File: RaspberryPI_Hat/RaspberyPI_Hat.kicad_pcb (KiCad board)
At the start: 2 copper layers, 65 x 56 mm, 17 parts, among them P1 Raspberry_PI, P2 CONN_01X02, P3 UEXT, U1 CAT24C32WI-GT3, U2 TSOP382

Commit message: Добавено реле
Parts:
- added P4: RAS-05-15, myfootprint:RAS-05-15, F.Cu at (107.0, 107.8)
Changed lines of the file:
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@@
 (kicad_pcb (version 4) (host pcbnew 4.0.2-stable)
   (general
-    (links 48)
-    (no_connects 48)
+    (links 44)
+    (no_connects 44)
     (area 97.924999 68.524999 163.075001 124.675001)
     (thickness 1.6)
@@
     (tracks 0)
     (zones 0)
-    (modules 17)
-    (nets 35)
+    (modules 18)
+    (nets 40)
   )
   (page A4)
@@
   (net 33 "Net-(C2-Pad1)")
   (net 34 "Net-(D1-Pad2)")
+  (net 35 "Net-(P4-Pad1)")
+  (net 36 "Net-(P4-Pad2)")
+  (net 37 "Net-(P4-Pad3)")
+  (net 38 "Net-(P4-Pad4)")
+  (net 39 "Net-(P4-Pad5)")
   (net_class Default "This is the default net class."
     (clearance 0.2)
@@
     (add_net "Net-(P1-Pad8)")
     (add_net "Net-(P2-Pad1)")
+    (add_net "Net-(P4-Pad1)")
+    (add_net "Net-(P4-Pad2)")
+    (add_net "Net-(P4-Pad3)")
+    (add_net "Net-(P4-Pad4)")
+    (add_net "Net-(P4-Pad5)")
   )
   (module Mounting_Holes:MountingHole_2.7mm_M2.5_DIN965_Pad (layer F.Cu)
@@
       (net 33 "Net-(C2-Pad1)"))
   )
+  (module myfootprint:RAS-05-15 (layer F.Cu)
+    (at 107 107.85 90)
+    (fp_text reference P4 (at 4.25 7.5 180) (layer F.SilkS)
+      (effects (font (size 1 1) (thickness 0.15)))
+    )
+    (fp_text value RAS-05-15 (at 1.27 -1.27 90) (layer F.Fab)
+      (effects (font (size 1 1) (thickness 0.15)))
+    )
+    (fp_line (start -5.5 15) (end -5.5 0) (layer F.SilkS) (width 0.15))
+    (fp_line (start 15.5 0) (end 15.5 15) (layer F.SilkS) (width 0.15))
+    (fp_line (start -5.5 15) (end 15.5 15) (layer F.SilkS) (width 0.15))
+    (fp_line (start -5.5 0) (end 15.5 0) (layer F.SilkS) (width 0.15))
+    (pad 1 thru_hole circle (at -2.1 1.5 90) (size 2.3 2.3) (drill 1.3) (layers *.Cu *.Mask F.SilkS)
+      (net 35 "Net-(P4-Pad1)"))
+    (pad 2 thru_hole circle (at 10.1 1.5 90) (size 2.3 2.3) (drill 1.3) (layers *.Cu *.Mask F.SilkS)
+      (net 36 "Net-(P4-Pad2)"))
+    (pad 3 thru_hole circle (at -2.1 13.5 90) (size 2.3 2.3) (drill 1.3) (layers *.Cu *.Mask F.SilkS)
+      (net 37 "Net-(P4-Pad3)"))
+    (pad 4 thru_hole circle (at 10.1 13.5 90) (size 2.3 2.3) (drill 1.3) (layers *.Cu *.Mask F.SilkS)
+      (net 38 "Net-(P4-Pad4)"))
+    (pad 5 thru_hole circle (at 12.1 7.5 90) (size 2.3 2.3) (drill 1.3) (layers *.Cu *.Mask F.SilkS)
+      (net 39 "Net-(P4-Pad5)"))
+  )
   (dimension 45 (width 0.3) (layer B.Adhes)

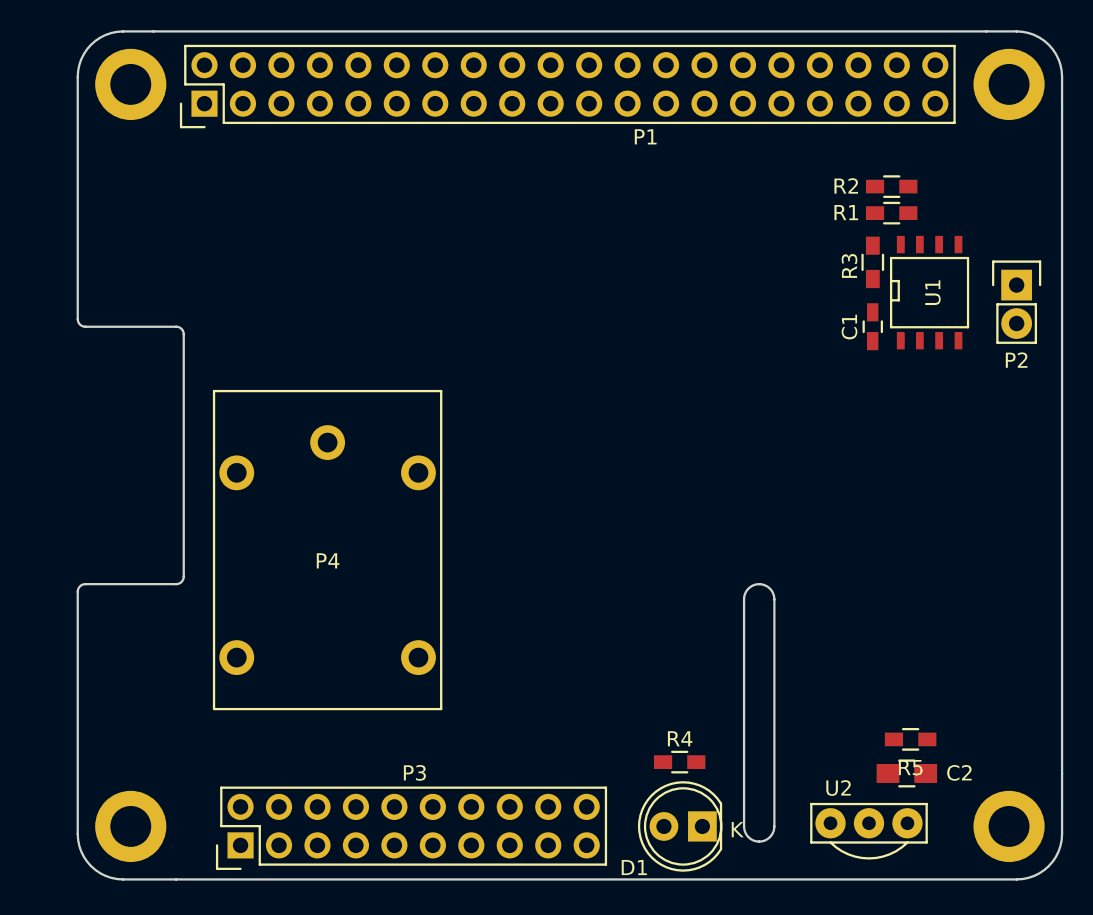
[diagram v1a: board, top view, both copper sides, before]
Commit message: Промяна на UEXT на 2x05 корпус
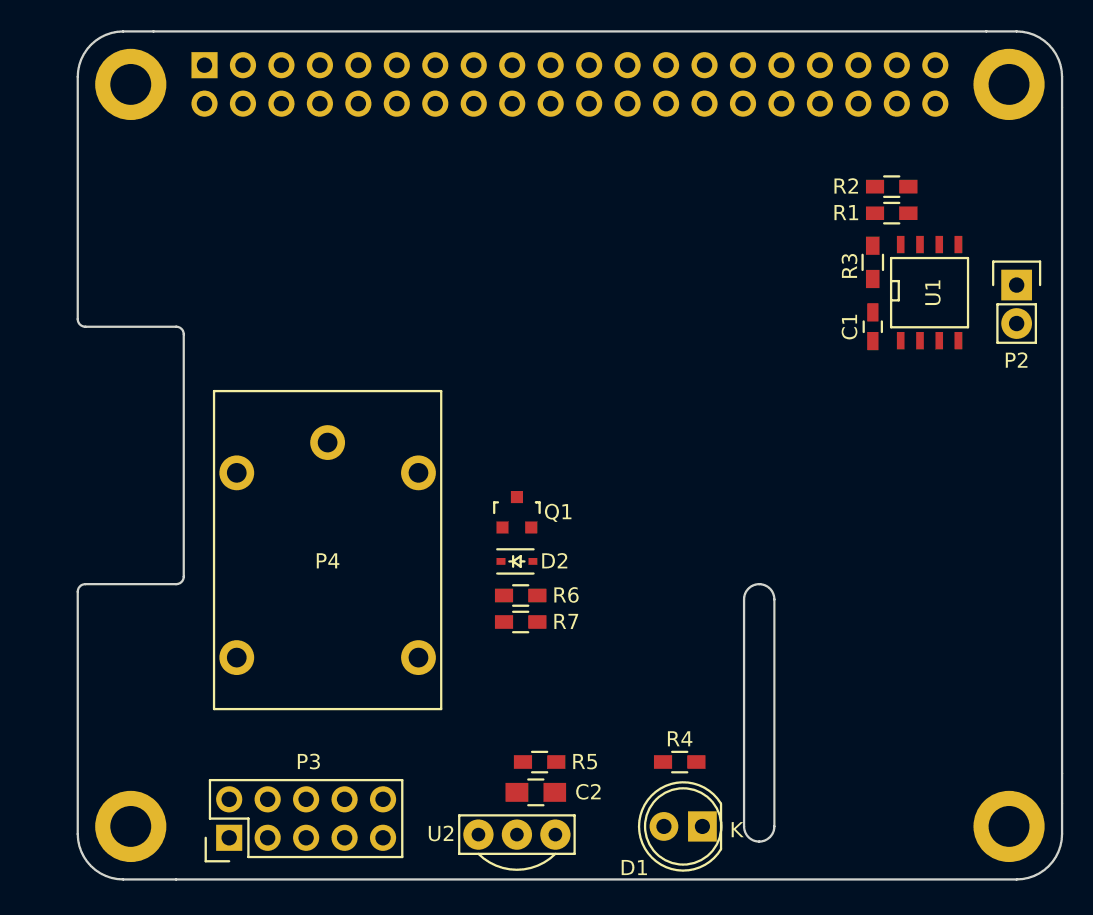
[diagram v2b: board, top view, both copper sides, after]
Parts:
- added D2: 1N4148, Diodes_SMD:SOD-323, F.Cu at (127.0, 103.6)
- added Q1: BC817, TO_SOT_Packages_SMD:SOT-23, F.Cu at (127.0, 100.3)
- added R6: 10K, Resistors_SMD:R_0603_HandSoldering, F.Cu at (127.2, 105.8)
- added R7: 2.2K, Resistors_SMD:R_0603_HandSoldering, F.Cu at (127.2, 107.6)
- C2: value 1.0 -> 10.0
- D1: value IR -> TSAL4600
- P1: moved to B.Cu
- P3: footprint Pin_Headers:Pin_Header_Straight_2x10 -> Pin_Headers:Pin_Header_Straight_2x05
- moved R5 24.5 mm to (128.5, 116.8)
- moved C2 24.5 mm to (128.2, 118.8)
- moved U2 23.3 mm to (127.0, 119.1)
- moved P3 0.90 mm to (108.0, 121.8)
- turned P1 to 270 degrees
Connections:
- P1 pad 2: Net-(P1-Pad2) -> +5V
- P1 pad 4: Net-(P1-Pad4) -> +5V
- P4 pad 2: Net-(P4-Pad2) -> +5V

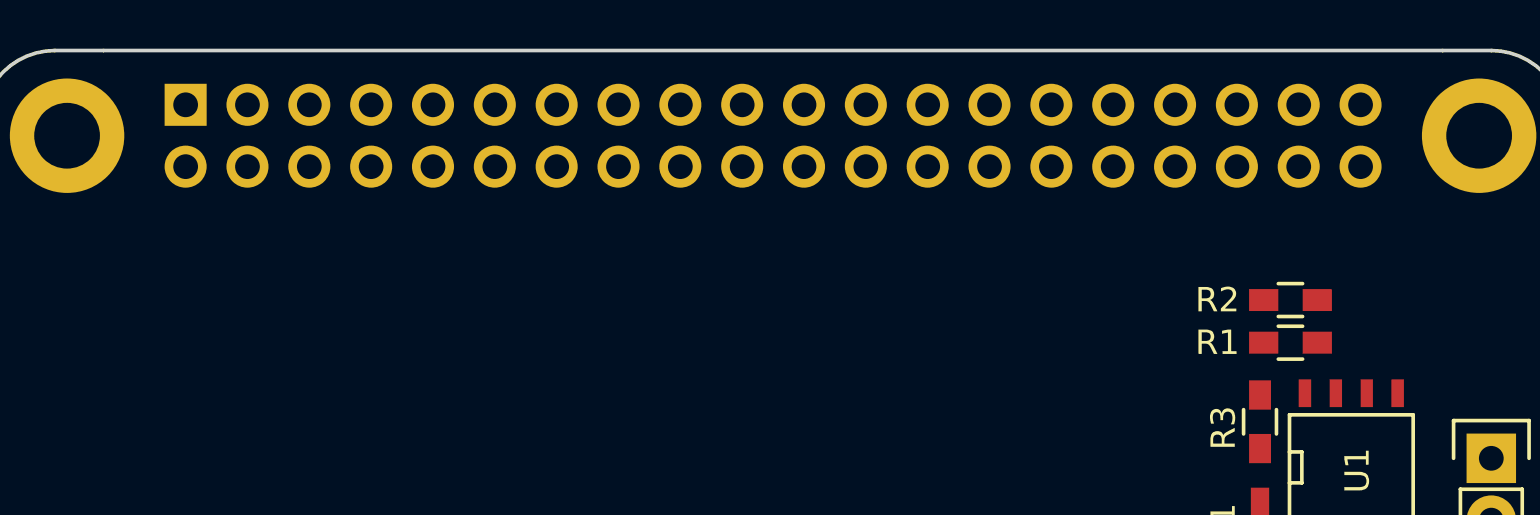
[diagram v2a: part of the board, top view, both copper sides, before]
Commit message: Обърнат конектор 2x20
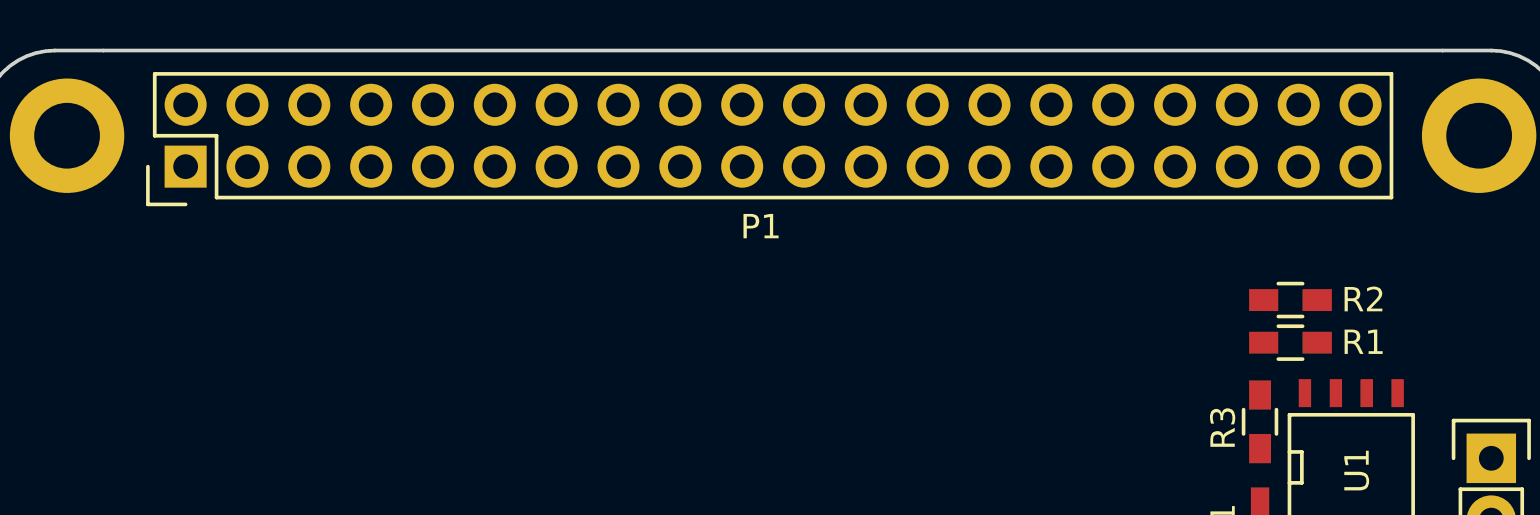
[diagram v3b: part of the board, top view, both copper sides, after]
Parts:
- P1: moved to F.Cu
- turned P1 to 90 degrees

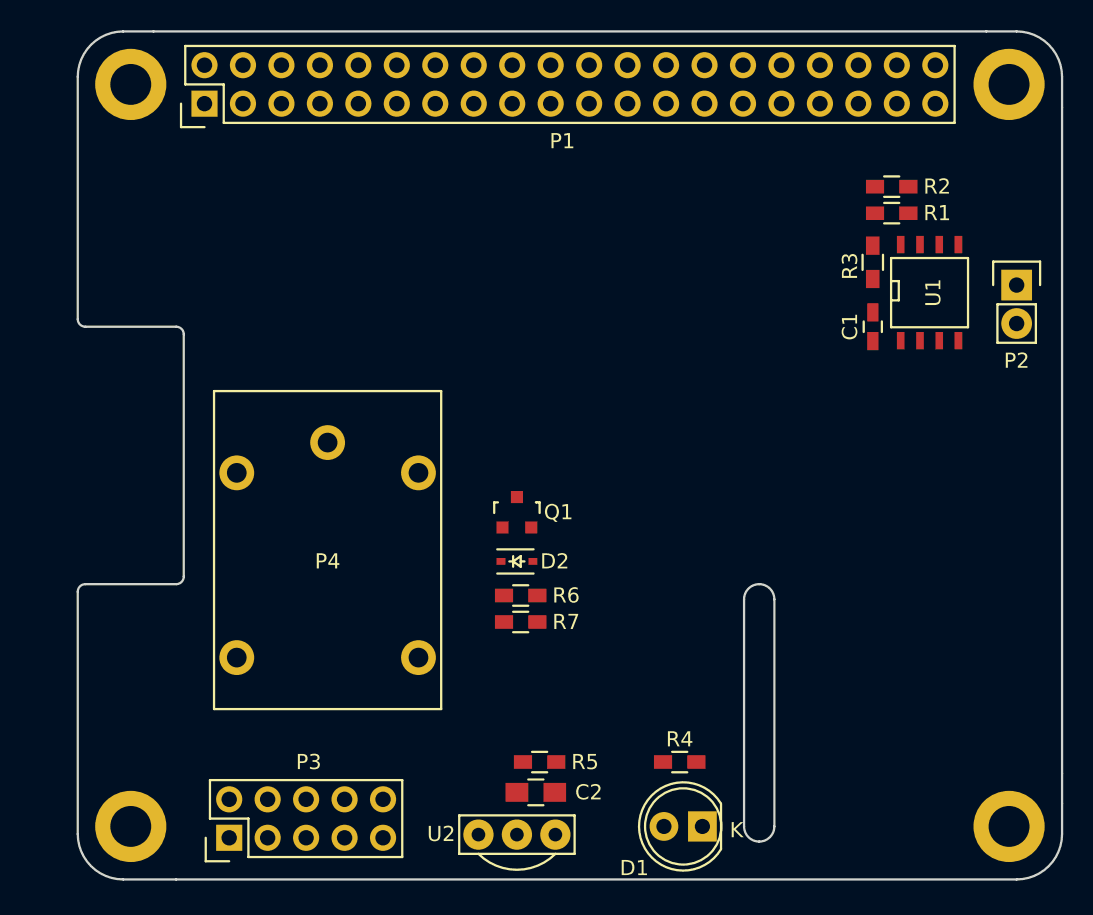
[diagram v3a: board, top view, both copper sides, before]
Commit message: Добавено LCD
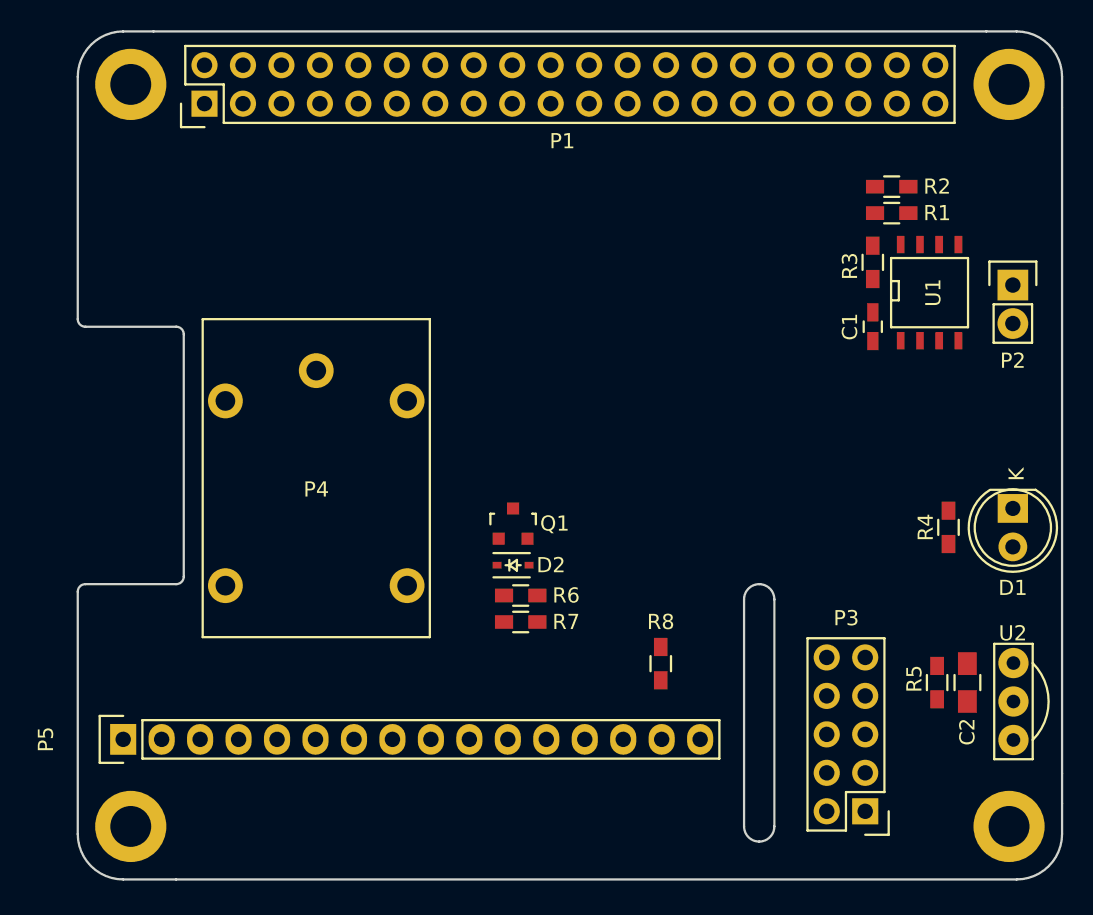
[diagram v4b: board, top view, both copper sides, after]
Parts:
- added P5: LCD_16x2, Pin_Headers:Pin_Header_Straight_1x16, F.Cu at (101.0, 115.3)
- added R8: 470, Resistors_SMD:R_0603_HandSoldering, F.Cu at (136.5, 110.3)
- moved P3 42.0 mm to (150.0, 120.1), turned to 180 degrees
- moved U2 30.9 mm to (157.2, 112.8), turned to 90 degrees
- moved C2 29.4 mm to (156.8, 111.6), turned to 270 degrees
- moved D1 29.3 mm to (159.8, 100.1), turned to 270 degrees
- moved R5 26.8 mm to (154.8, 111.6), turned to 270 degrees
- moved R4 23.6 mm to (155.5, 101.3), turned to 90 degrees
- moved P4 4.81 mm to (106.2, 103.1)
- moved Q1 0.79 mm to (126.8, 101.1)
- moved D2 0.35 mm to (126.8, 103.8)
- moved P2 0.25 mm to (159.8, 85.3)
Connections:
- P1 pad 11: Net-(P1-Pad11) -> /D5
- P1 pad 13: Net-(P1-Pad13) -> /D6
- P1 pad 15: Net-(P1-Pad15) -> /D7
- P1 pad 16: Net-(P1-Pad16) -> /D4
- P1 pad 18: Net-(P1-Pad18) -> /EN
- P1 pad 22: Net-(P1-Pad22) -> /RS
- U2 pad 1: Net-(P1-Pad22) -> Net-(P1-Pad37)

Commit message: Добавени хедъри за сензори, бутон, зумер
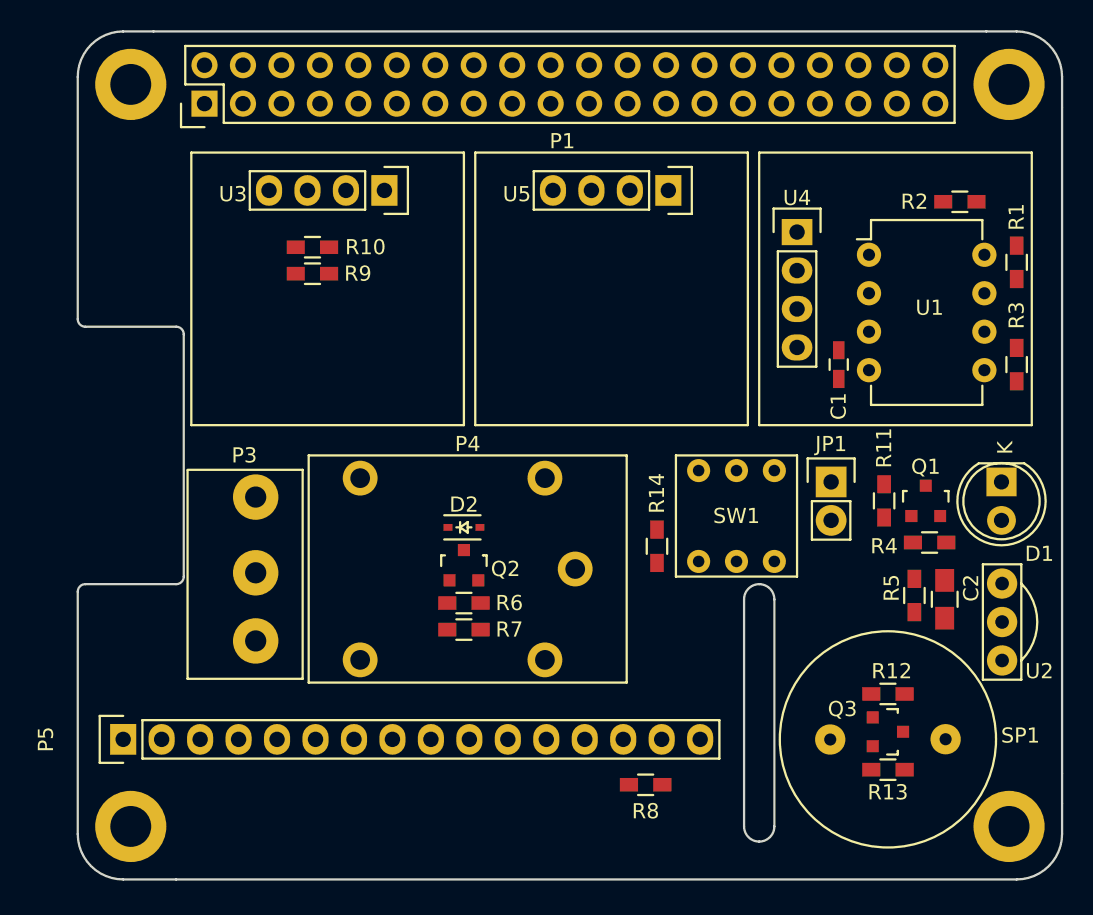
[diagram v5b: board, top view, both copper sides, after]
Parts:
- removed P2: CONN_01X02, Pin_Headers:Pin_Header_Straight_1x02
- added JP1: JUMPER, Pin_Headers:Pin_Header_Straight_1x02, F.Cu at (147.8, 98.3)
- added Q2: BC817, TO_SOT_Packages_SMD:SOT-23, F.Cu at (123.5, 103.8)
- added Q3: BC817, TO_SOT_Packages_SMD:SOT-23, F.Cu at (151.5, 114.8)
- added R10: 3.9K, Resistors_SMD:R_0603_HandSoldering, F.Cu at (113.5, 82.8)
- added R11: 2.2K, Resistors_SMD:R_0603_HandSoldering, F.Cu at (151.2, 99.6)
- added R12: 2.2K, Resistors_SMD:R_0603_HandSoldering, F.Cu at (151.5, 112.3)
- added R13: 1K, Resistors_SMD:R_0603_HandSoldering, F.Cu at (151.5, 117.3)
- added R14: 470, Resistors_SMD:R_0603_HandSoldering, F.Cu at (136.2, 102.6)
- added R9: 3.9K, Resistors_SMD:R_0603_HandSoldering, F.Cu at (113.5, 84.6)
- added SP1: BUZZER, myfootprint:PIEZO-MCKPI-G1410, F.Cu at (151.5, 115.3)
- added SW1: SW_PUSH, myfootprint:PUSH_P1, F.Cu at (141.5, 100.6)
- added U3: I2C_SENS_1, myfootprint:I2C_SENS_1, F.Cu at (123.5, 76.6)
- added U4: I2C_SENS_1, myfootprint:I2C_SENS_1, F.Cu at (143.0, 76.6)
- added U5: I2C_SENS_1, myfootprint:I2C_SENS_1, F.Cu at (142.2, 76.6)
- P3: value UEXT -> CONN_01X03; footprint Pin_Headers:Pin_Header_Straight_2x05 -> myfootprint:KLEMA_1x3
- U1: footprint SMD_Packages:SOIC-8-N -> Housings_DIP:DIP-8_W7.62mm
- moved P3 42.2 mm to (113.2, 99.3), turned to 270 degrees
- moved Q1 27.3 mm to (154.0, 99.6)
- moved P4 14.1 mm to (118.8, 96.6), turned to 0 degrees
- moved R3 11.7 mm to (160.0, 90.6), turned to 270 degrees
- moved R1 8.87 mm to (160.0, 83.8), turned to 270 degrees
- moved R8 8.06 mm to (135.5, 118.3), turned to 180 degrees
- moved R5 5.94 mm to (153.2, 105.8)
- moved C2 5.70 mm to (155.2, 106.1)
- moved U2 5.30 mm to (156.5, 107.6)
- moved U1 4.72 mm to (150.2, 83.3)
- moved R2 4.61 mm to (156.2, 79.8), turned to 180 degrees
- moved D2 4.10 mm to (123.5, 101.3)
- moved R6 3.78 mm to (123.5, 106.3)
- moved R7 3.78 mm to (123.5, 108.1)
- moved C1 3.36 mm to (148.2, 90.6)
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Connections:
- D1 pad 1: GND -> Net-(D1-Pad1)
- P3 pad 1: +3V3 -> Net-(P3-Pad1)
- P3 pad 2: GND -> Net-(P3-Pad2)
- P3 pad 3: Net-(P1-Pad8) -> Net-(P3-Pad3)
- P4 pad 1: Net-(P4-Pad1) -> Net-(P3-Pad3)
- P4 pad 3: Net-(P4-Pad3) -> Net-(P3-Pad2)
- P4 pad 5: Net-(P4-Pad5) -> Net-(P3-Pad1)
- Q1 pad 2: Net-(D2-Pad2) -> GND
- Q1 pad 3: GND -> Net-(D1-Pad1)
- R4 pad 2: Net-(P1-Pad32) -> +5V
- R5 pad 1: Net-(C2-Pad1) -> +3V3
- R5 pad 2: +3V3 -> Net-(C2-Pad1)
- R7 pad 1: Net-(Q1-Pad1) -> Net-(Q2-Pad1)
